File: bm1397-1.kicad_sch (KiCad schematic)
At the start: 101 parts, among them IC1 BM1397_mode1, J3 Conn_01x05, U3 SN74LVC1T45DBVR, U5 MCP1824T-1802E, U5 SN74LVC1T45DBVR, U6 MCP1824T-0802E, U8 SN74LVC1T45DBVR, X1 OT322525MJBA4SL

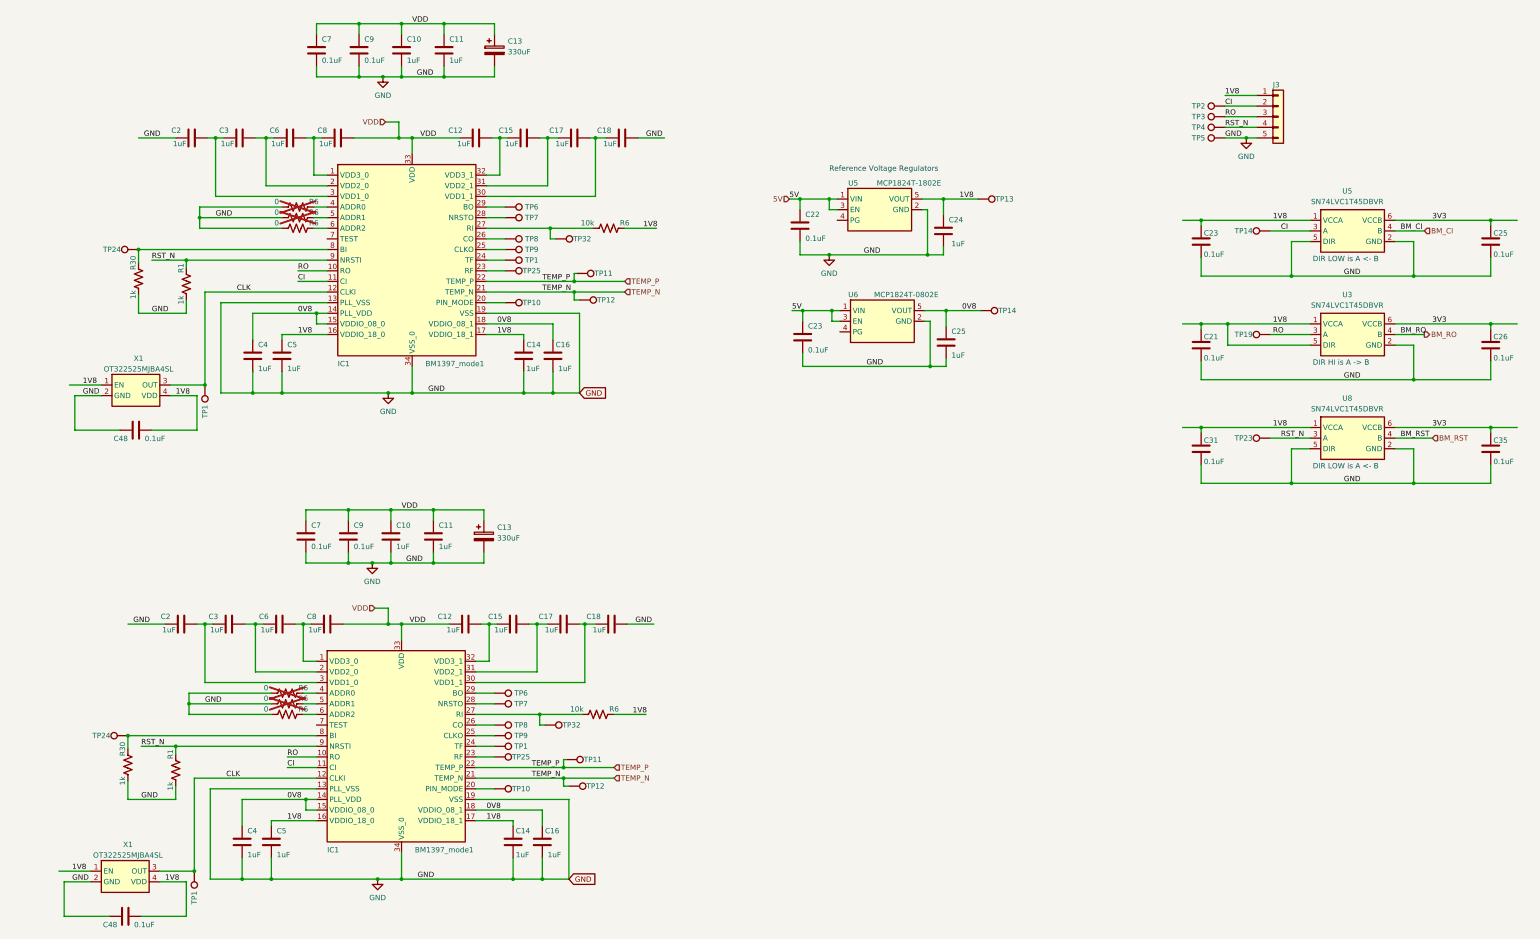
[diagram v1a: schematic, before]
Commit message: starting to sort out the asic data connections
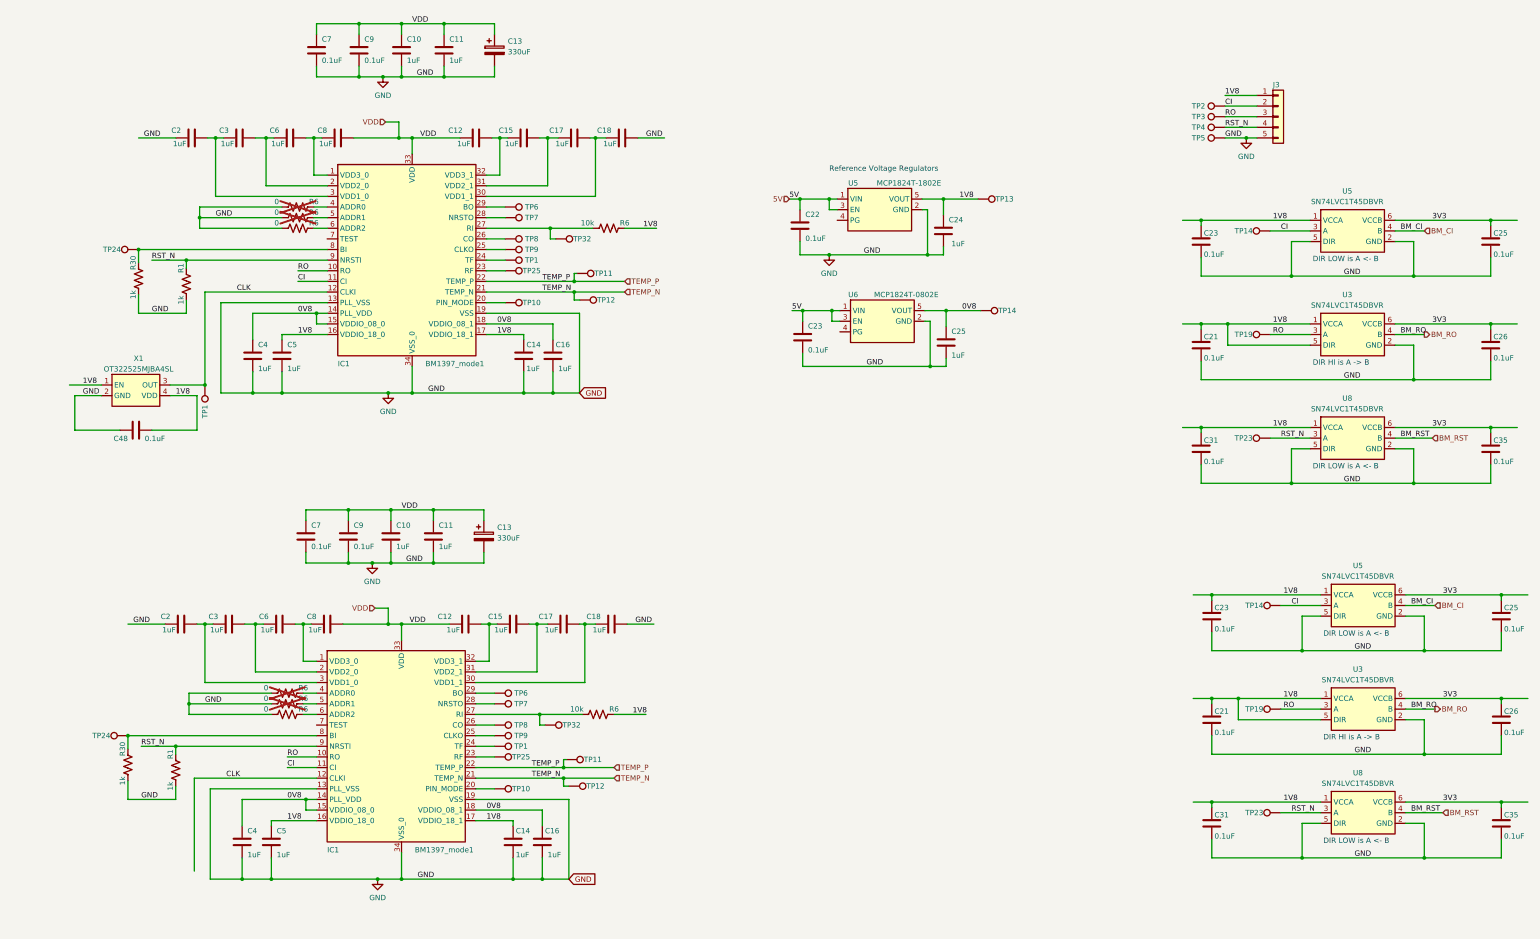
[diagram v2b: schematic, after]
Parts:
- removed C48: 311-3342-1-ND, Capacitor_SMD:C_0402_1005Metric, symbol Device:C
- removed TP1: TestPoint, TestPoint:TestPoint_Pad_D1.5mm, symbol Connector:TestPoint
- removed X1: OT322525MJBA4SL, lcsc:OSC-SMD_4P-L3.2-W2.5-BL, symbol lcsc:OT322525MJBA4SL
- added C21, C23, C25, C26, C31, C35: 311-3342-1-ND, Capacitor_SMD:C_0402_1005Metric, symbol Device:C
- added TP14, TP19, TP23: TestPoint, TestPoint:TestPoint_Pad_D1.5mm, symbol Connector:TestPoint
- added U3, U5, U8: SN74LVC1T45DBVR, lcsc:SOT-23-6_L2.9-W1.6-P0.95-LS2.8-BR, symbol lcsc:SN74LVC1T45DBVR
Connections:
- net 1V8: now also C21.1, C23.1, C31.1, U3.1 (VCCA), U3.5 (DIR), U5.1 (VCCA), U8.1 (VCCA)
- net 3V3: now also C25.1, C26.1, C35.1, U3.6 (VCCB), U5.6 (VCCB), U8.6 (VCCB)
- net BM_CI: now also U5.4 (B)
- net BM_RO: now also U3.4 (B)
- net BM_RST: now also U8.4 (B)
- net CI: now also TP14.1, U5.3 (A)
- net GND: now also C21.2, C23.2, C25.2, C26.2, C31.2, C35.2, U3.2 (GND), U5.2 (GND), U5.5 (DIR), U8.2 (GND), U8.5 (DIR)
- net RO: now also TP19.1, U3.3 (A)
- net RST_N: now also TP23.1, U8.3 (A)

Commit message: connected up power and data to ASICs in schematic
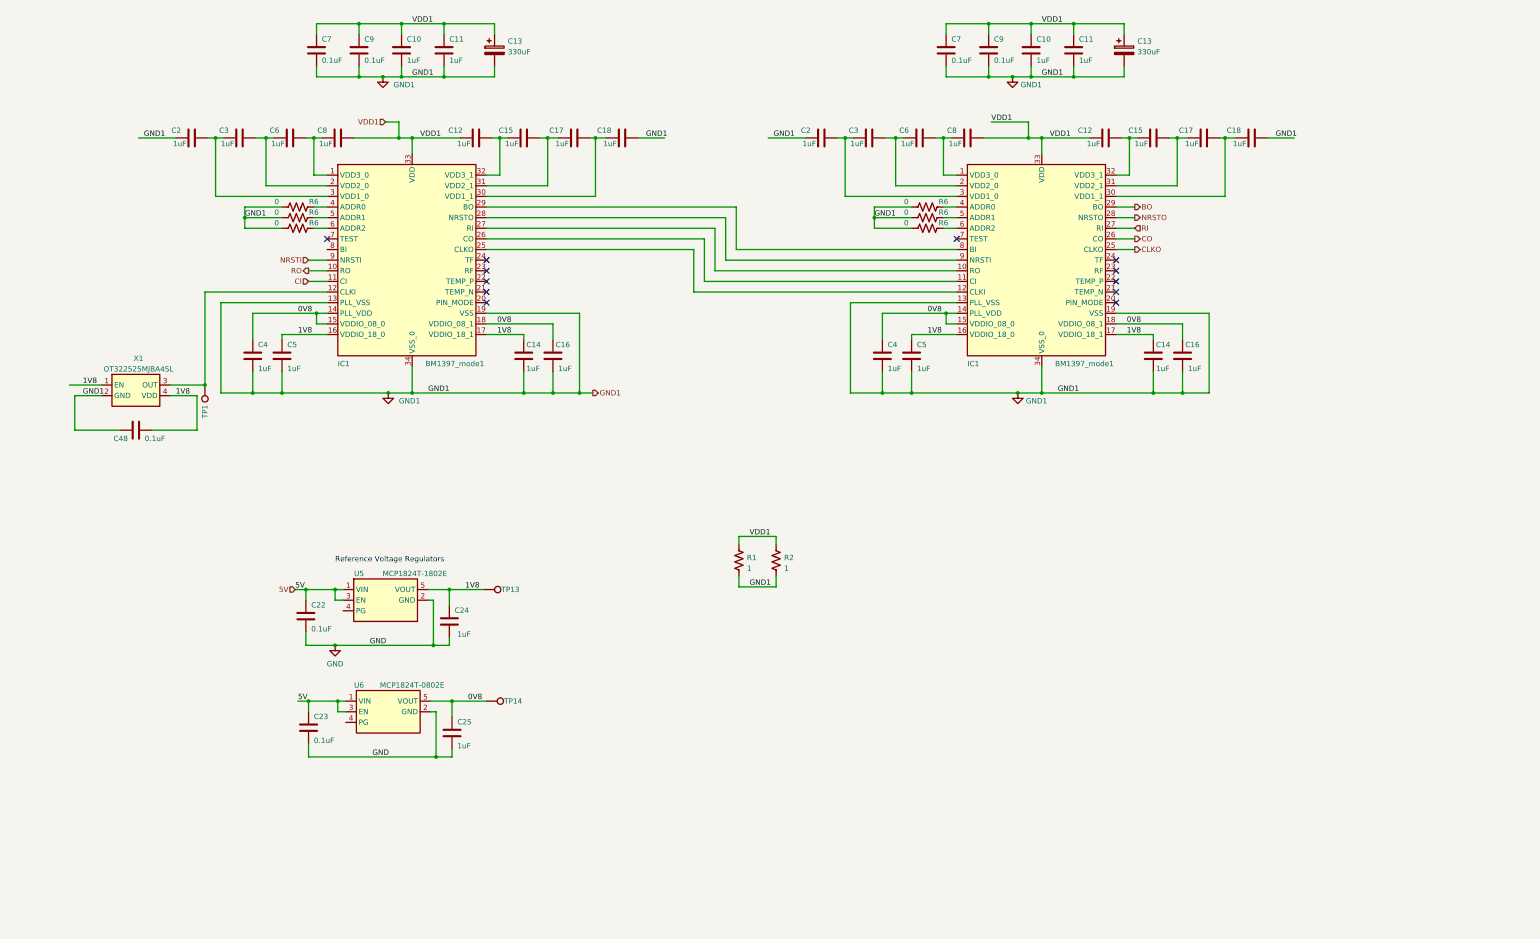
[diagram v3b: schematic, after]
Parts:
- removed C21 (x2), C23 (x2), C25 (x2), C26 (x2), C31 (x2), C35 (x2): 311-3342-1-ND, Capacitor_SMD:C_0402_1005Metric, symbol Device:C
- removed J3: Conn_01x05, Connector_PinHeader_2.54mm:PinHeader_1x05_P2.54mm_Vertical, symbol Connector_Generic:Conn_01x05
- removed R1 (x2), R30 (x2): 1k, Resistor_SMD:R_0402_1005Metric, symbol Device:R_US
- removed R6 (x2): 10k, Resistor_SMD:R_0402_1005Metric, symbol Device:R_US
- removed TP1 (x2), TP10 (x2), TP11 (x2), TP12 (x2), TP14 (x2), TP19 (x2), TP2, TP23 (x2), TP24 (x2), TP25 (x2), TP3, TP32 (x2), TP4, TP5, TP6 (x2), TP7 (x2), TP8 (x2), TP9 (x2): TestPoint, TestPoint:TestPoint_Pad_D1.5mm, symbol Connector:TestPoint
- removed U3 (x2), U5 (x2), U8 (x2): SN74LVC1T45DBVR, lcsc:SOT-23-6_L2.9-W1.6-P0.95-LS2.8-BR, symbol lcsc:SN74LVC1T45DBVR
- added R1, R2: 1, Resistor_SMD:R_2512_6332Metric, symbol Device:R_US
- R6: now fitted
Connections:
- net CI: no longer IC1.11 (CI)
- net GND: now also R1.2, R2.2
- net RO: no longer IC1.10 (RO)
- net at IC1.27 (RI): now also IC1.10 (RO)
- net at IC1.8 (BI): now also IC1.29 (BO)
- net at IC1.25 (CLKO): now also IC1.12 (CLKI)
- net at IC1.26 (CO): now also IC1.11 (CI)
- net at IC1.28 (NRSTO): now also IC1.9 (NRSTI)
- net RI: now reaches IC1.27 (RI)
- net CLKO: now reaches IC1.25 (CLKO)
- net BO: now reaches IC1.29 (BO)
- net CO: now reaches IC1.26 (CO)
- net NRSTO: now reaches IC1.28 (NRSTO)
- net CLK: no longer names the net of IC1.12 (CLKI), TP1.1, X1.3 (OUT)
- net CLK: no longer IC1.12 (CLKI)
- net RST_N renamed NRSTI
- net NRSTI: no longer IC1.9 (NRSTI)
- net TEMP_N: no longer names the net of IC1.21 (TEMP_N)
- net TEMP_N: no longer IC1.21 (TEMP_N)
- net TEMP_P: no longer names the net of IC1.22 (TEMP_P)
- net TEMP_P: no longer IC1.22 (TEMP_P)
- net VDD renamed VDD1
- net VDD1: now also R1.1, R2.1
- no-connect marks 0 -> 12
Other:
- note removed: "DIR HI is A -> B"
- note removed: "DIR LOW is A <- B"
- moved on the sheet: C10, C11, C12, C13, C14, C15, C16, C17, C18, C2, C22, C23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

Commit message: fixed the floating gnd net issue. started placement
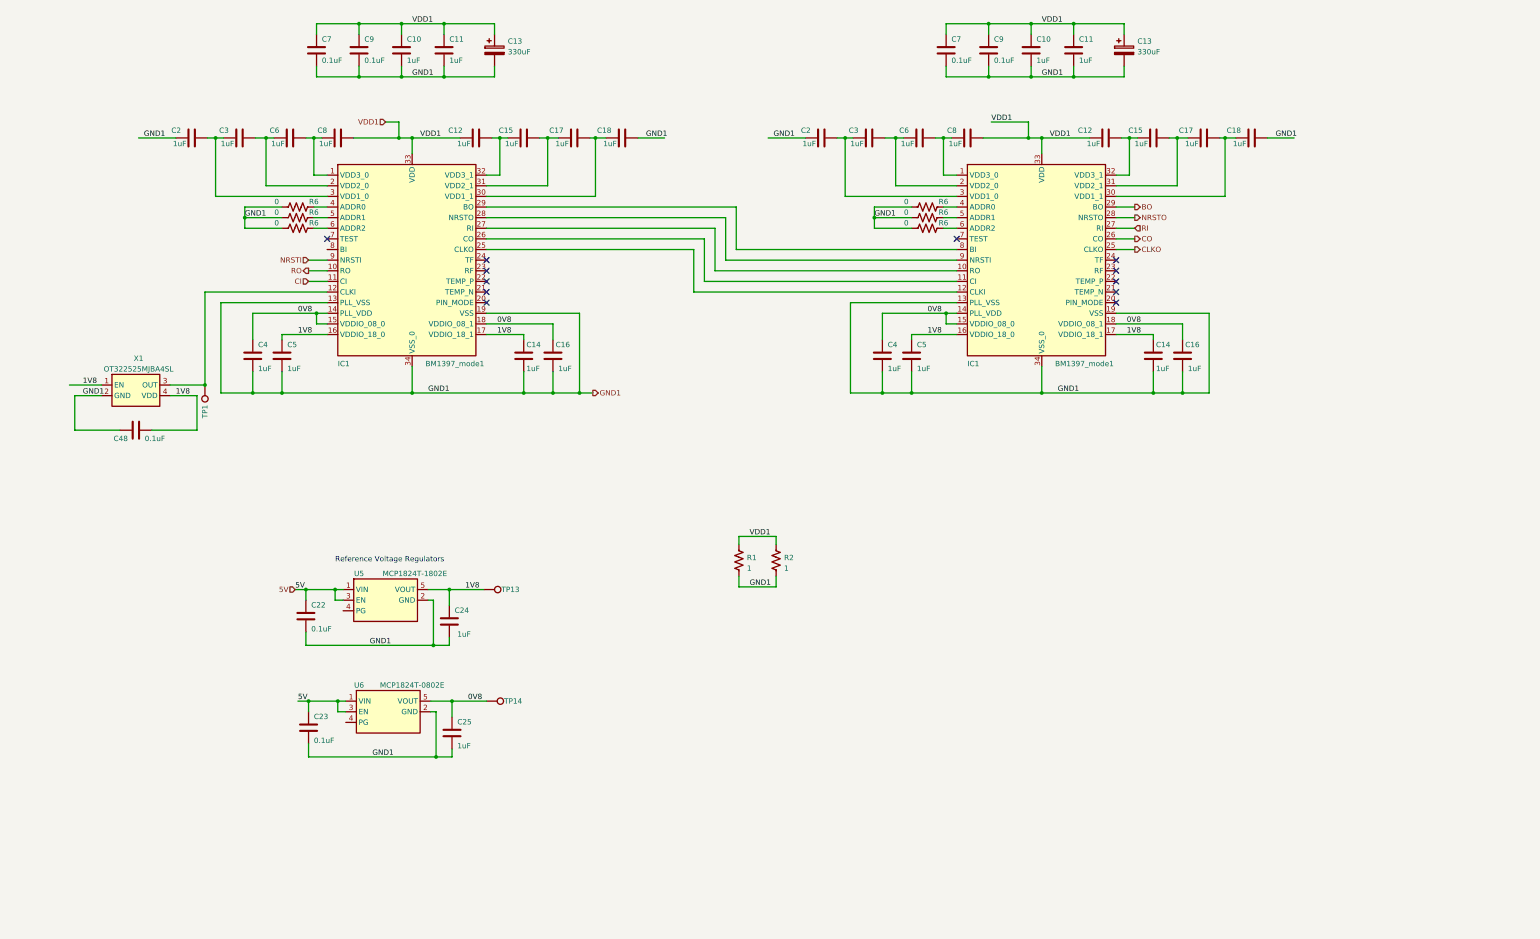
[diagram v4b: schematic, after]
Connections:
- net GND renamed GND1

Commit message: some more placements, added level shifters..
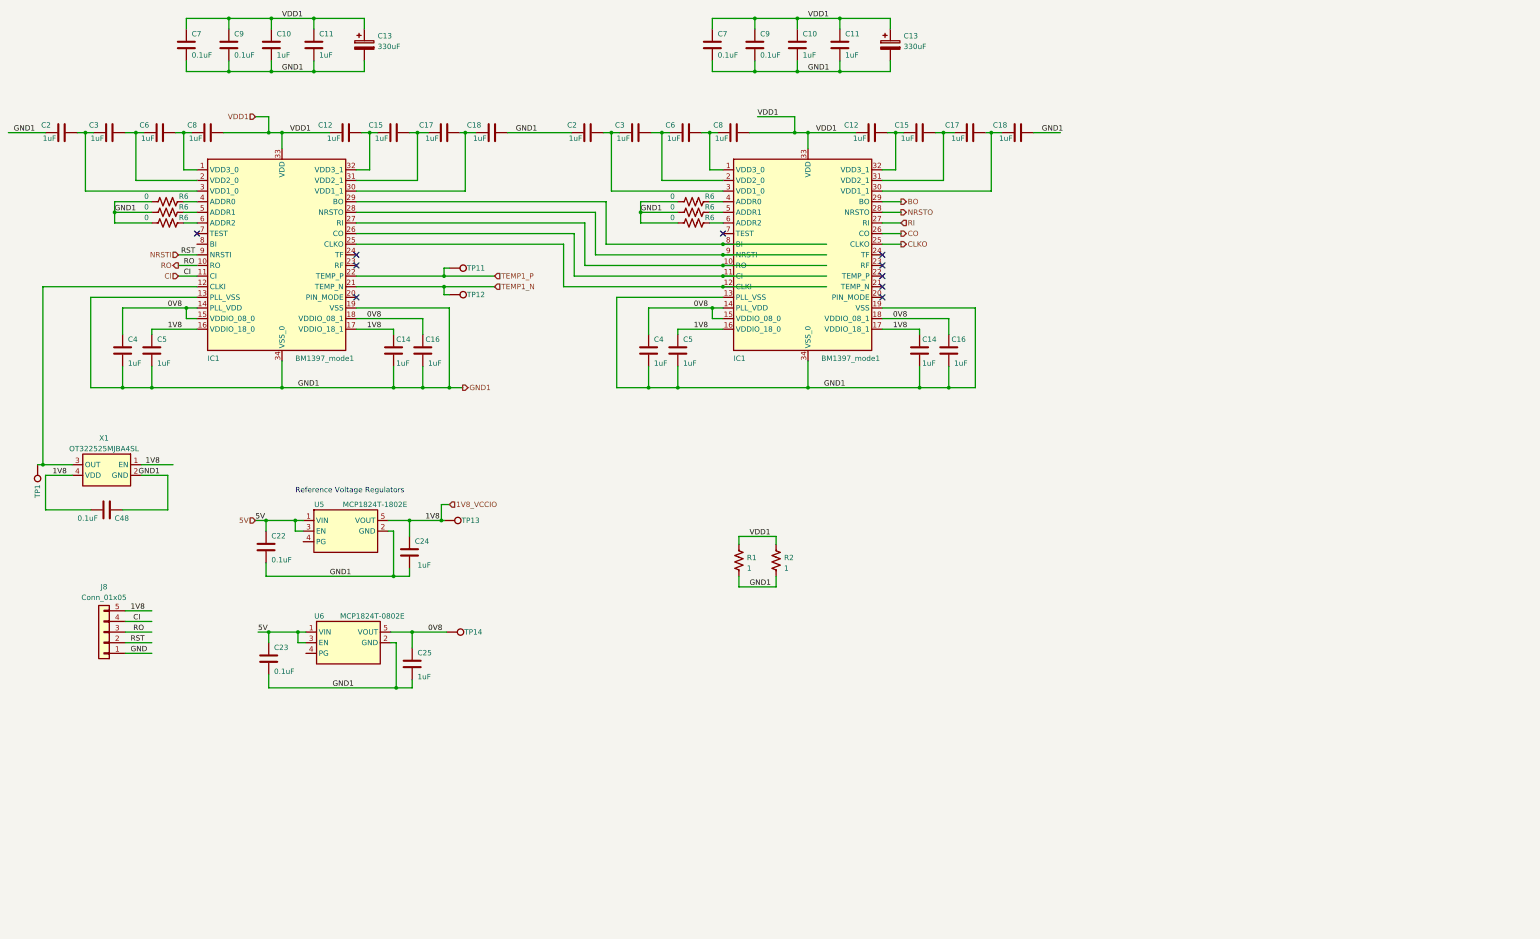
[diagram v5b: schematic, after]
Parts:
- added J8: Conn_01x05, Connector_PinHeader_2.54mm:PinHeader_1x05_P2.54mm_Vertical, symbol Connector_Generic:Conn_01x05
- added TP11, TP12: TestPoint, TestPoint:TestPoint_Pad_D1.5mm, symbol Connector:TestPoint
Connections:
- net CI: now also J8.4 (Pin_4)
- net NRSTI: now also J8.2 (Pin_2)
- net RO: now also J8.3 (Pin_3)
- net TEMP1_N: now reaches IC1.21 (TEMP_N)
- net TEMP1_N: now also TP12.1
- net TEMP1_P: now reaches IC1.22 (TEMP_P)
- net TEMP1_P: now also TP11.1
- net 1V8 renamed 1V8_VCCIO
- net 1V8_VCCIO: now also J8.5 (Pin_5)
- new net GND: J8.1 (Pin_1)
- no-connect marks 12 -> 10
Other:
- moved on the sheet: C10, C11, C12, C13, C14, C15, C16, C17, C18, C2, C22, C23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
